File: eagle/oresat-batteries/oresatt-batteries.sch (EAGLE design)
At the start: 63 parts, among them U1 TCAN330, U2 STM32F042K6, X1 16MHz

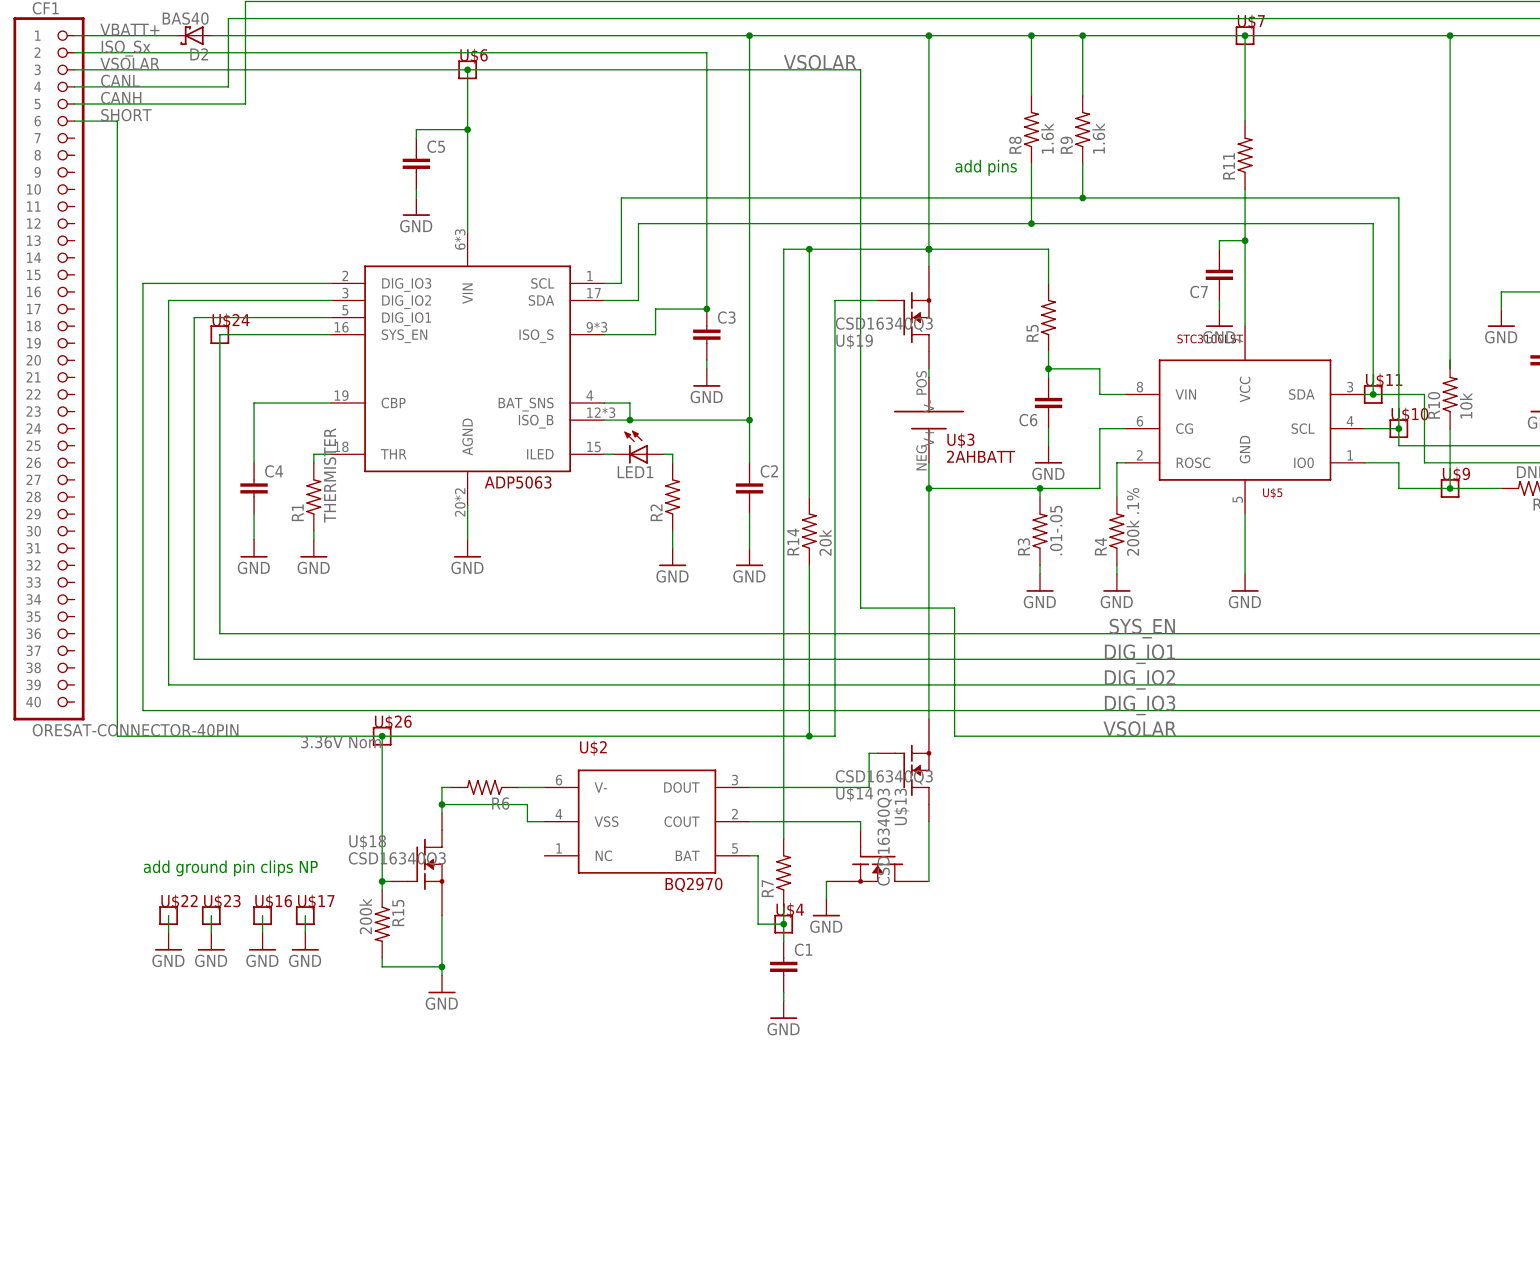
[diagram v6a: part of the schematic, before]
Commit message: Replaced Shutdown with new circuitry that will actually work... maybe.
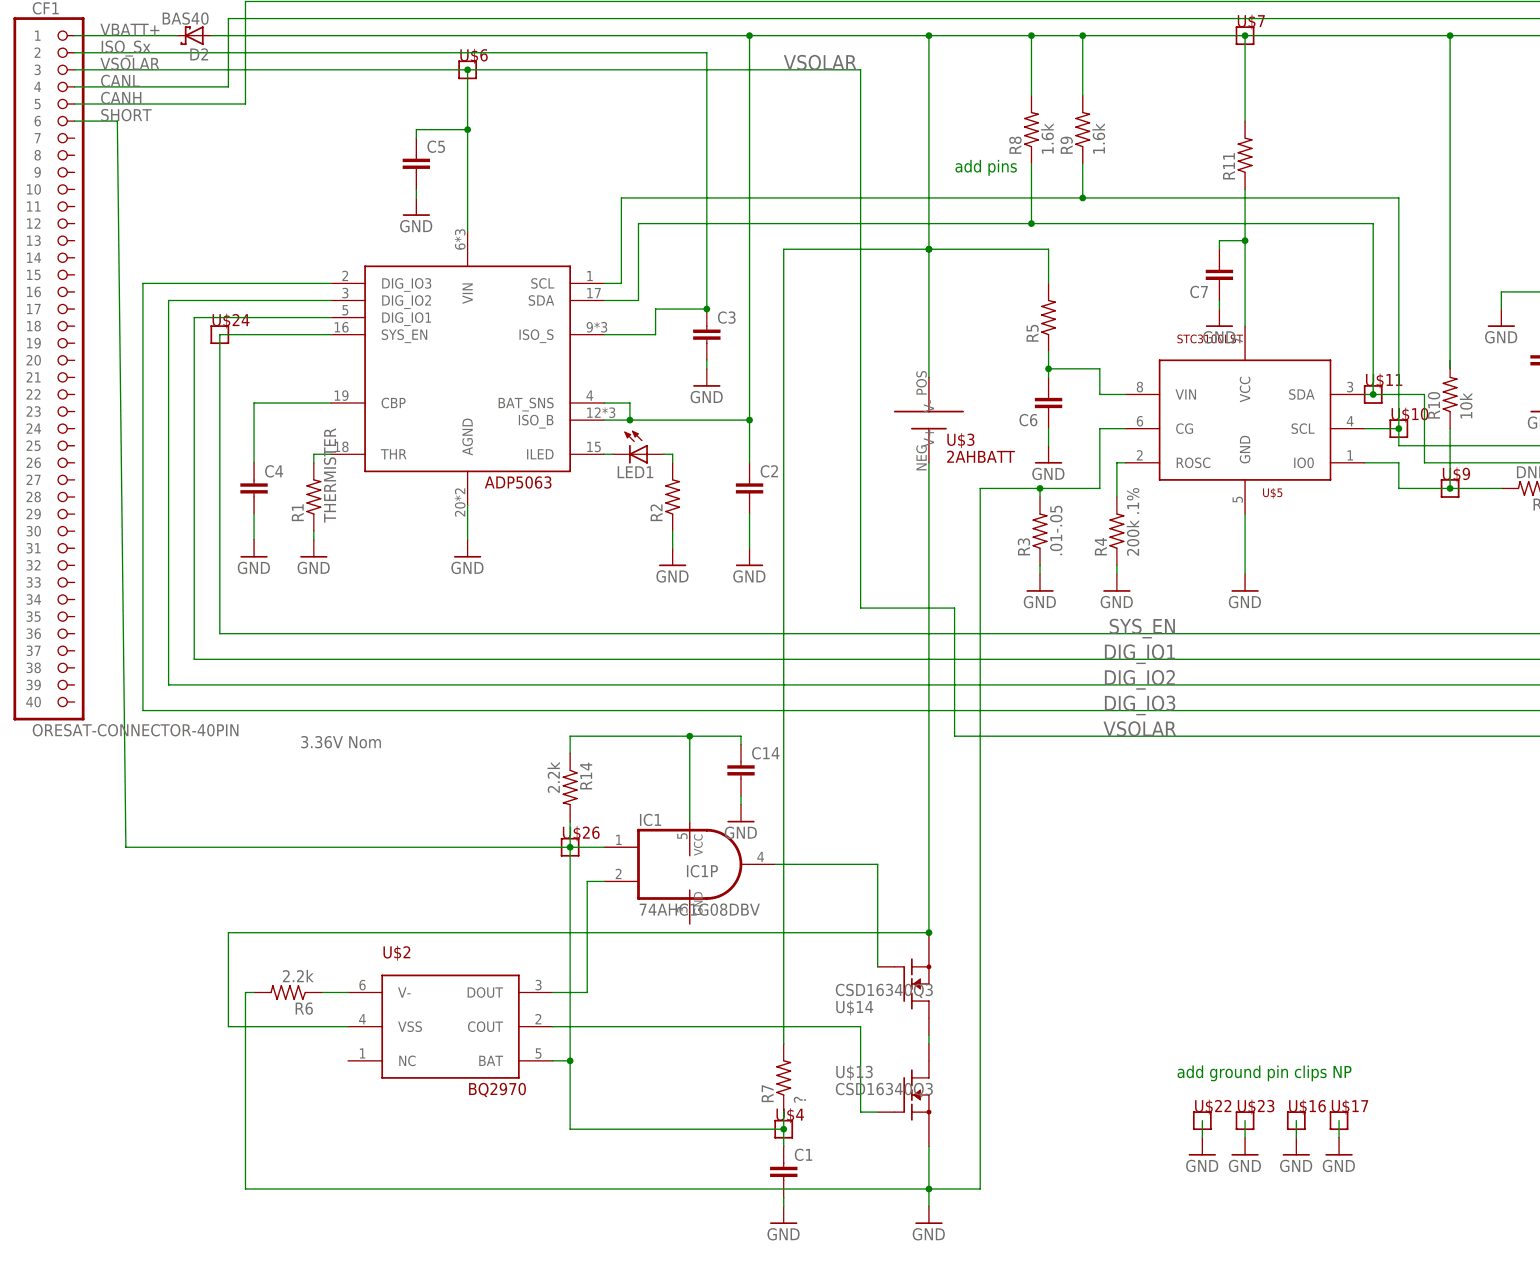
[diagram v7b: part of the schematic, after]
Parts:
- removed R15: 200k, rcl:R-US_R0603
- removed U$18, U$19: CSD16340Q3, oresat-batteries:CSD16340Q3
- added C14: (no value), rcl:C-EUC0603
- added IC1: 74AHC1G08DBV, 74xx-little-us:74AHC1G08DBV
- R14: value 20k -> 2.2k
- R6: value (none) -> 2.2k
- R7: value (none) -> ?
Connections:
- removed net BATTHICUT: U$19.D, U$3.V+
- removed net BQKILL: R6.2, U$18.D, U$2.VSS
- removed net DOUT: U$14.G, U$2.DOUT
- removed net SHORTBAR: CF1.6, R14.1, R15.1, U$18.G, U$19.G
- new net N$3: IC1A.O, U$14.G
- new net N$5: IC1A.I1, U$2.DOUT
- new net N$6: C14.1, IC1P.VCC, R14.1
- net BQBAT: now also CF1.6, IC1A.I0, R14.2
- net GND: now also C14.2, R3.2, R6.2, U$5.CG; no longer R15.2, U$18.S
- net STC_CG: now also U$2.VSS; no longer R3.2, U$5.CG
- net VBATT+: now also U$3.V+; no longer R14.2, U$19.S
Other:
- moved on the sheet: C1, R14, R6, R7, U$13, U$14, U$16, U$17, U$2, U$22, U$23, U$26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

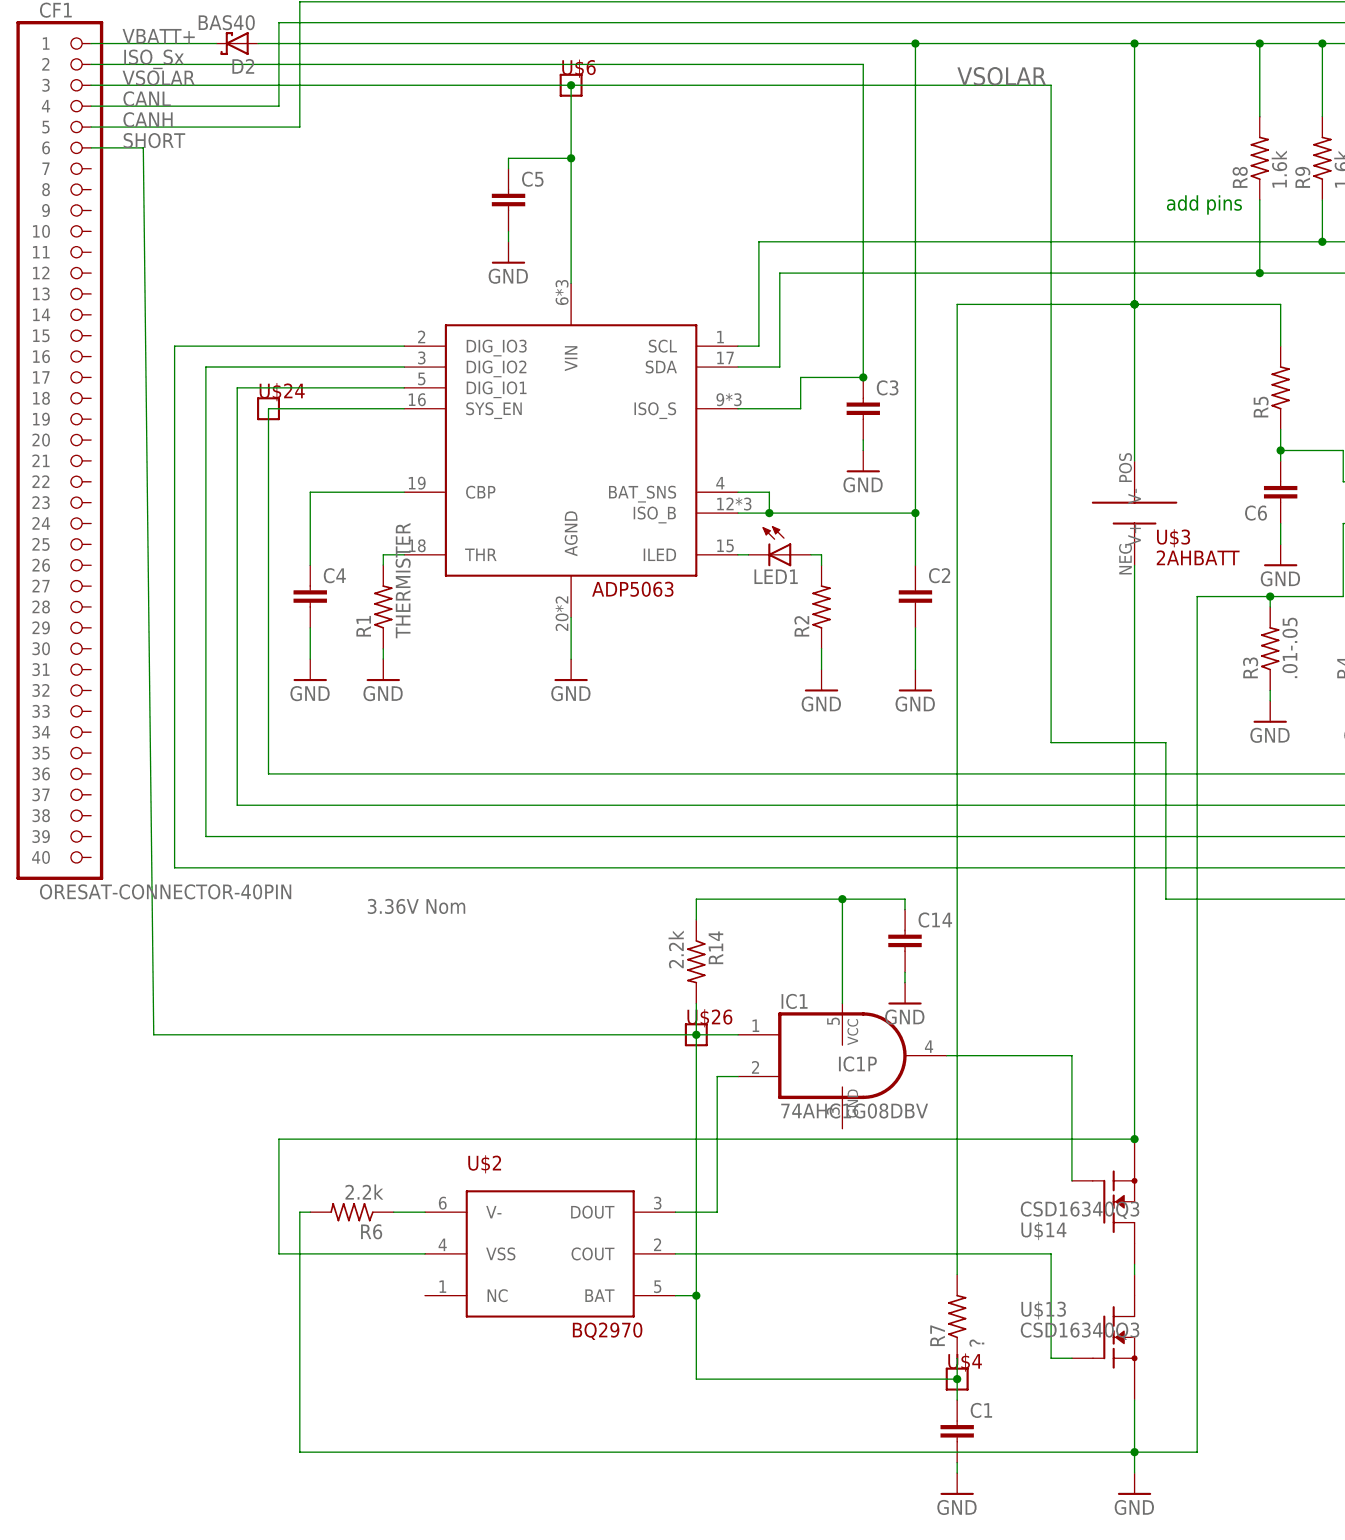
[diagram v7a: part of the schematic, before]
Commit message: Cleaned up schematic
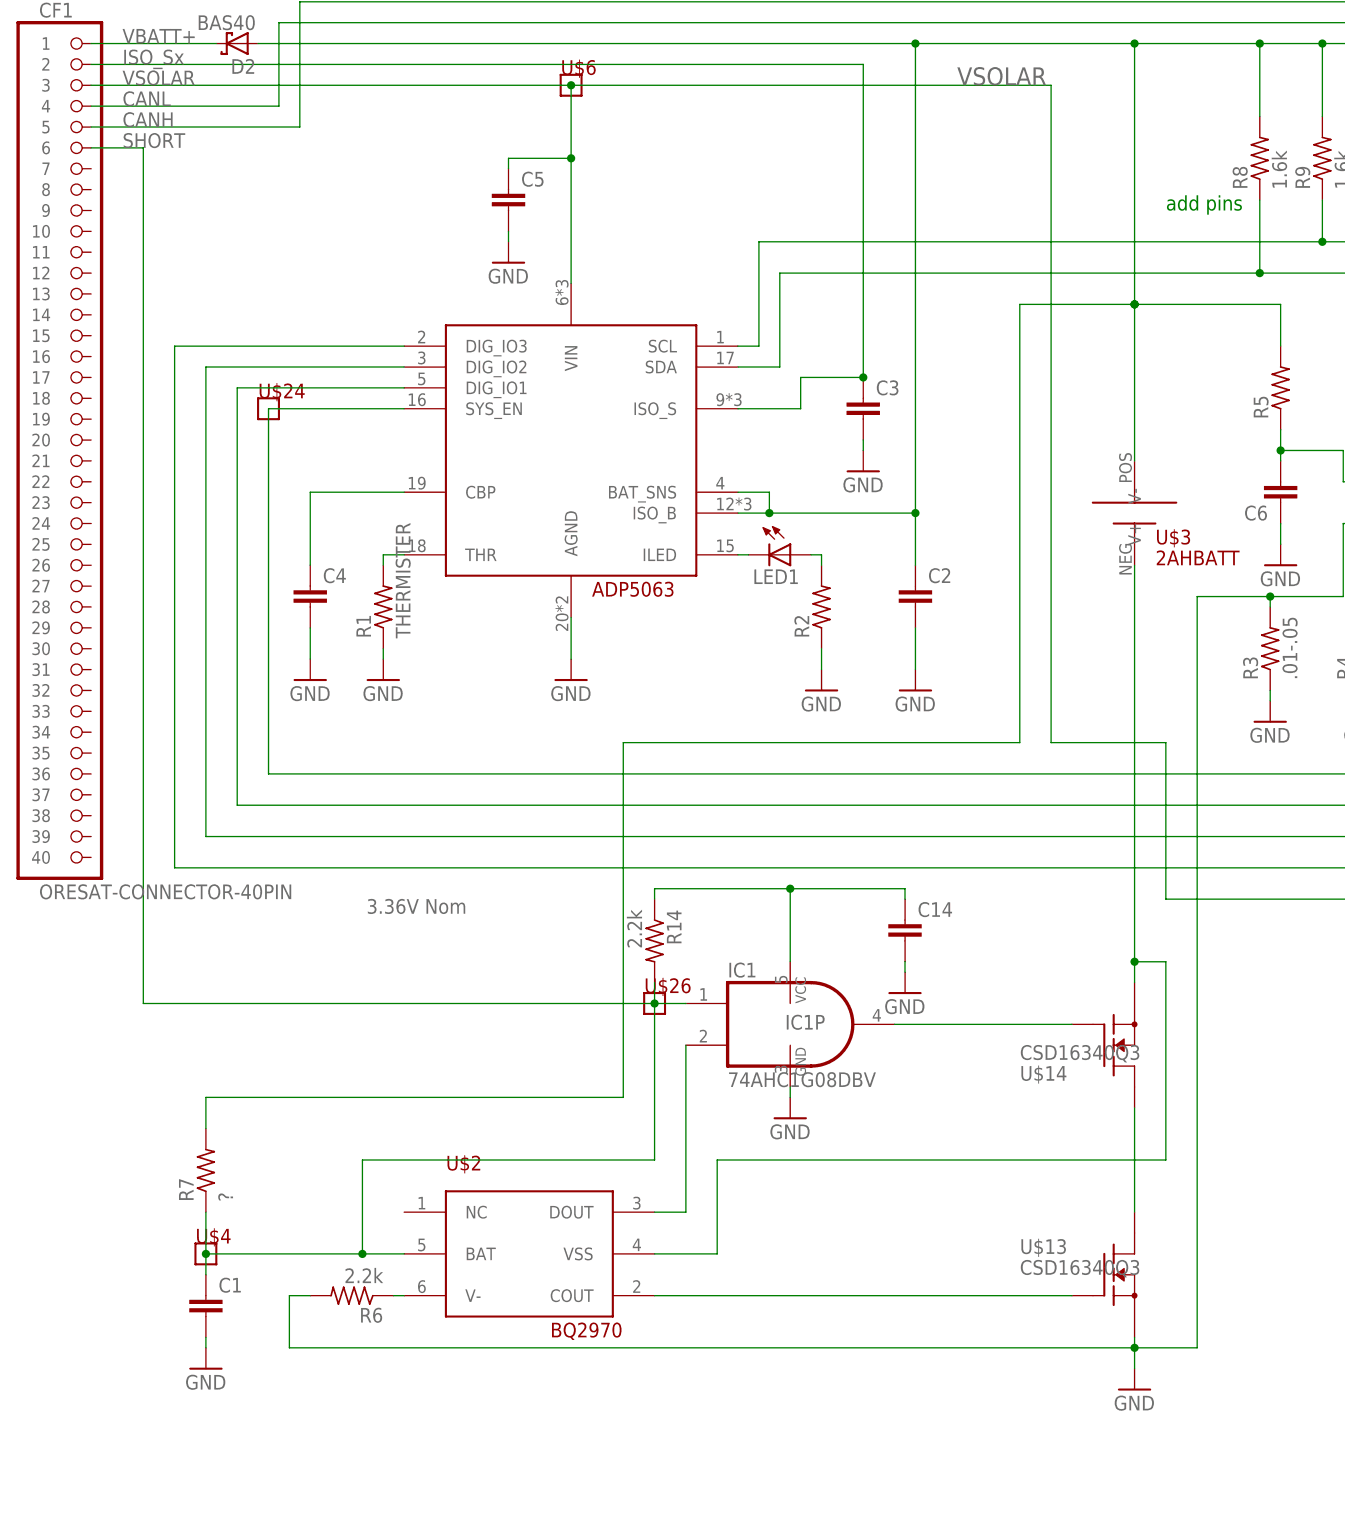
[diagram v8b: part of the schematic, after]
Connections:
- net GND: now also IC1P.GND
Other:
- moved on the sheet: C1, C14, IC1, IC1P, R14, R6, R7, U$13, U$14, U$2, U$26, U$4
